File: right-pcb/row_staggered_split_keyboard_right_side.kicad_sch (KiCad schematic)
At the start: 11 parts, among them J1 Conn_01x02, U1 SN74LVC1T45DBV

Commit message: initial placement of switches and modifications from left to right
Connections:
- net COL7: now reaches A1.15 (MO)
- no-connect marks 7 -> 6
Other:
- sheet R2C6: file switch_with_LED_2U.kicad_sch -> switch_with_LED_1U5.kicad_sch
- sheet R3C1: file switch_with_LED_1U5.kicad_sch -> switch_with_LED_1U.kicad_sch
- sheet R4C1: file switch_with_LED_1U75.kicad_sch -> switch_with_LED_1U.kicad_sch
- sheet R4C6: file switch_with_LED_1U.kicad_sch -> switch_with_LED_1U75.kicad_sch
- sheet R5C1: file switch_with_LED_2U.kicad_sch -> switch_with_LED_1U.kicad_sch
- sheet R5C6: file switch_with_LED_1U.kicad_sch -> switch_with_LED_2U.kicad_sch
- sheet R6C0: file switch_with_LED_2U25.kicad_sch -> switch_with_LED_1U.kicad_sch
- sheet R6C1: file switch_with_LED_1U25.kicad_sch -> switch_with_LED_2U25.kicad_sch
- sheet R6C4: file switch_with_LED_2U25.kicad_sch -> switch_with_LED_1U25.kicad_sch
- note added: "CTL"
- note added: "F17"
- note removed: "SUPER"

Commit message: a bunch of DRC fixes and pcb work
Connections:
- net COL7: no longer names the net of A1.15 (MO)
- no-connect marks 6 -> 7

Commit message: Silkscreen cleanup and trace cleanup in prep for PCB review posting
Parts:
- J1: now left out of the parts list
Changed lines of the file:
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@@
 		(unit 1)
 		(exclude_from_sim no)
-		(in_bom yes)
+		(in_bom no)
 		(on_board yes)
 		(dnp no)

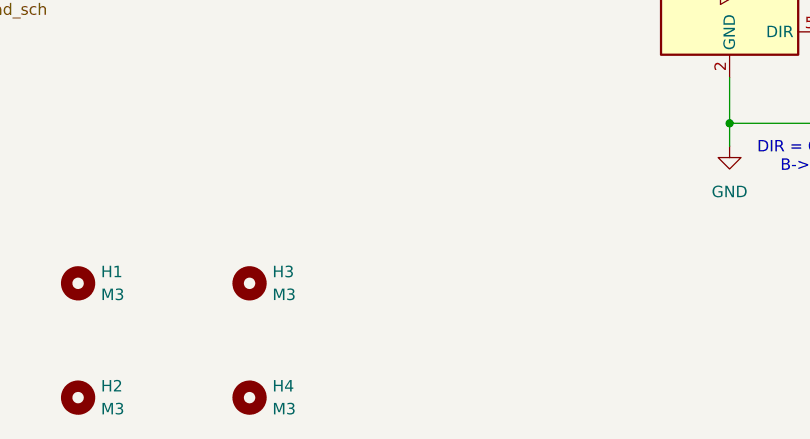
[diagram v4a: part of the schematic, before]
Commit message: adding mounting hole in center for additional support, and cleaning up tracks/zones
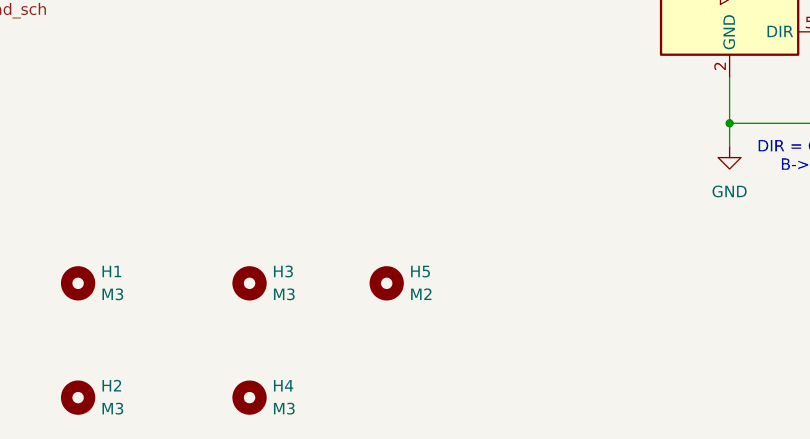
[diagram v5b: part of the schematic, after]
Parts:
- added H5: M2, MountingHole:MountingHole_2.2mm_M2, symbol Mechanical:MountingHole
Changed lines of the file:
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@@
+	)
+	(symbol
+		(lib_id "Mechanical:MountingHole")
+		(at 337.82 233.68 0)
+		(unit 1)
+		(body_style 1)
+		(exclude_from_sim no)
+		(in_bom no)
+		(on_board yes)
+		(in_pos_files no)
+		(dnp no)
+		(fields_autoplaced yes)
+		(property "Reference" "H5"
+			(at 340.36 232.4099 0)
+			(show_name no)
+			(do_not_autoplace no)
+			(effects
+				(font
+					(size 1.27 1.27)
+				)
+				(justify left)
+			)
+		)
+		(property "Value" "M2"
+			(at 340.36 234.9499 0)
+			(show_name no)
+			(do_not_autoplace no)
+			(effects
+				(font
+					(size 1.27 1.27)
+				)
+				(justify left)
+			)
+		)
+		(property "Footprint" "MountingHole:MountingHole_2.2mm_M2"
+			(at 337.82 233.68 0)
+			(hide yes)
+			(show_name no)
+			(do_not_autoplace no)
+			(effects
+				(font
+					(size 1.27 1.27)
+				)
+			)
+		)
+		(property "Datasheet" ""
+			(at 337.82 233.68 0)
+			(hide yes)
+			(show_name no)
+			(do_not_autoplace no)
+			(effects
+				(font
+					(size 1.27 1.27)
+				)
+			)
+		)
+		(property "Description" "Mounting Hole without connection"
+			(at 337.82 233.68 0)
+			(hide yes)
+			(show_name no)
+			(do_not_autoplace no)
+			(effects
+				(font
+					(size 1.27 1.27)
+				)
+			)
+		)
+		(instances
+			(project "row_staggered_split_keyboard_right_side"
+				(path "/cf145565-22e2-4e5a-8a27-915862c57a1b"
+					(reference "H5")
+					(unit 1)
+				)
+			)
+		)
 	)
 	(symbol
@@
 		(in_bom no)
 		(on_board yes)
-		(in_pos_files yes)
+		(in_pos_files no)
 		(dnp no)
 		(fields_autoplaced yes)
@@
 		(in_bom no)
 		(on_board yes)
-		(in_pos_files yes)
+		(in_pos_files no)
 		(dnp no)
 		(fields_autoplaced yes)
@@
 		(in_bom no)
 		(on_board yes)
-		(in_pos_files yes)
+		(in_pos_files no)
 		(dnp no)
 		(fields_autoplaced yes)
@@
 		(in_bom no)
 		(on_board yes)
-		(in_pos_files yes)
-		(dnp no)
-		(fields_autoplaced yes)
+		(in_pos_files no)
+		(dnp no)
+		(fields_autoplaced yes)
